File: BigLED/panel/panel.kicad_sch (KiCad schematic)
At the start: 29 parts, among them J1 Power, J2 LED PWR, J3 BTN1, J4 BTN2, J5 Spkr, U2 DAC7311xDCK, U3 NS4110B_C5334145

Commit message: Finist SCH for BigLED
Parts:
- added C12: 10.0, symbol Device:C
- added C13: 220x16v, symbol Device:C_Polarized
- added R5: 121, symbol Device:R
- added R6: 330, symbol Device:R
- added U4: LM1085-ADJ, symbol Regulator_Linear:LM1085-ADJ
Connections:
- net +3.3V: now also C13.1, R5.1, U4.2 (VO); no longer U1.2 (3Vo)
- net +5V: now also C12.1, U4.3 (VI)
- net GND: now also C12.2, C13.2, R6.2
- new net: R5.2, R6.1, U4.1 (ADJ)
- no-connect marks 0 -> 2

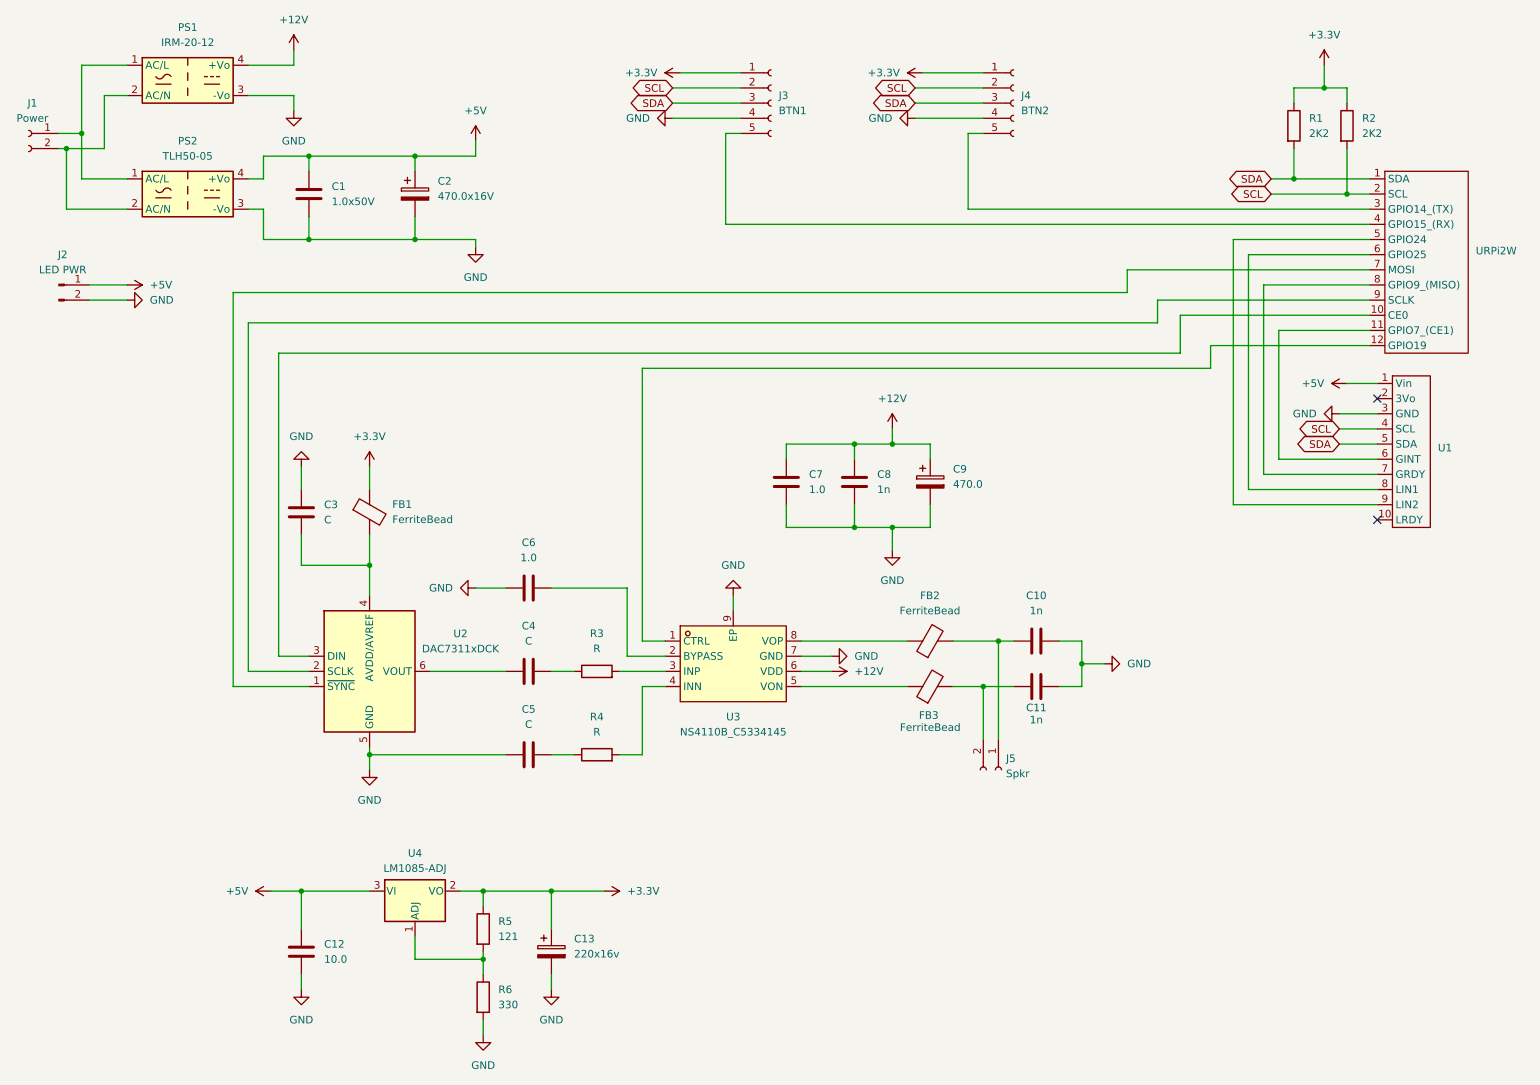
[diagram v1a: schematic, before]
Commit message: Converted BigLED to KiCAD v9
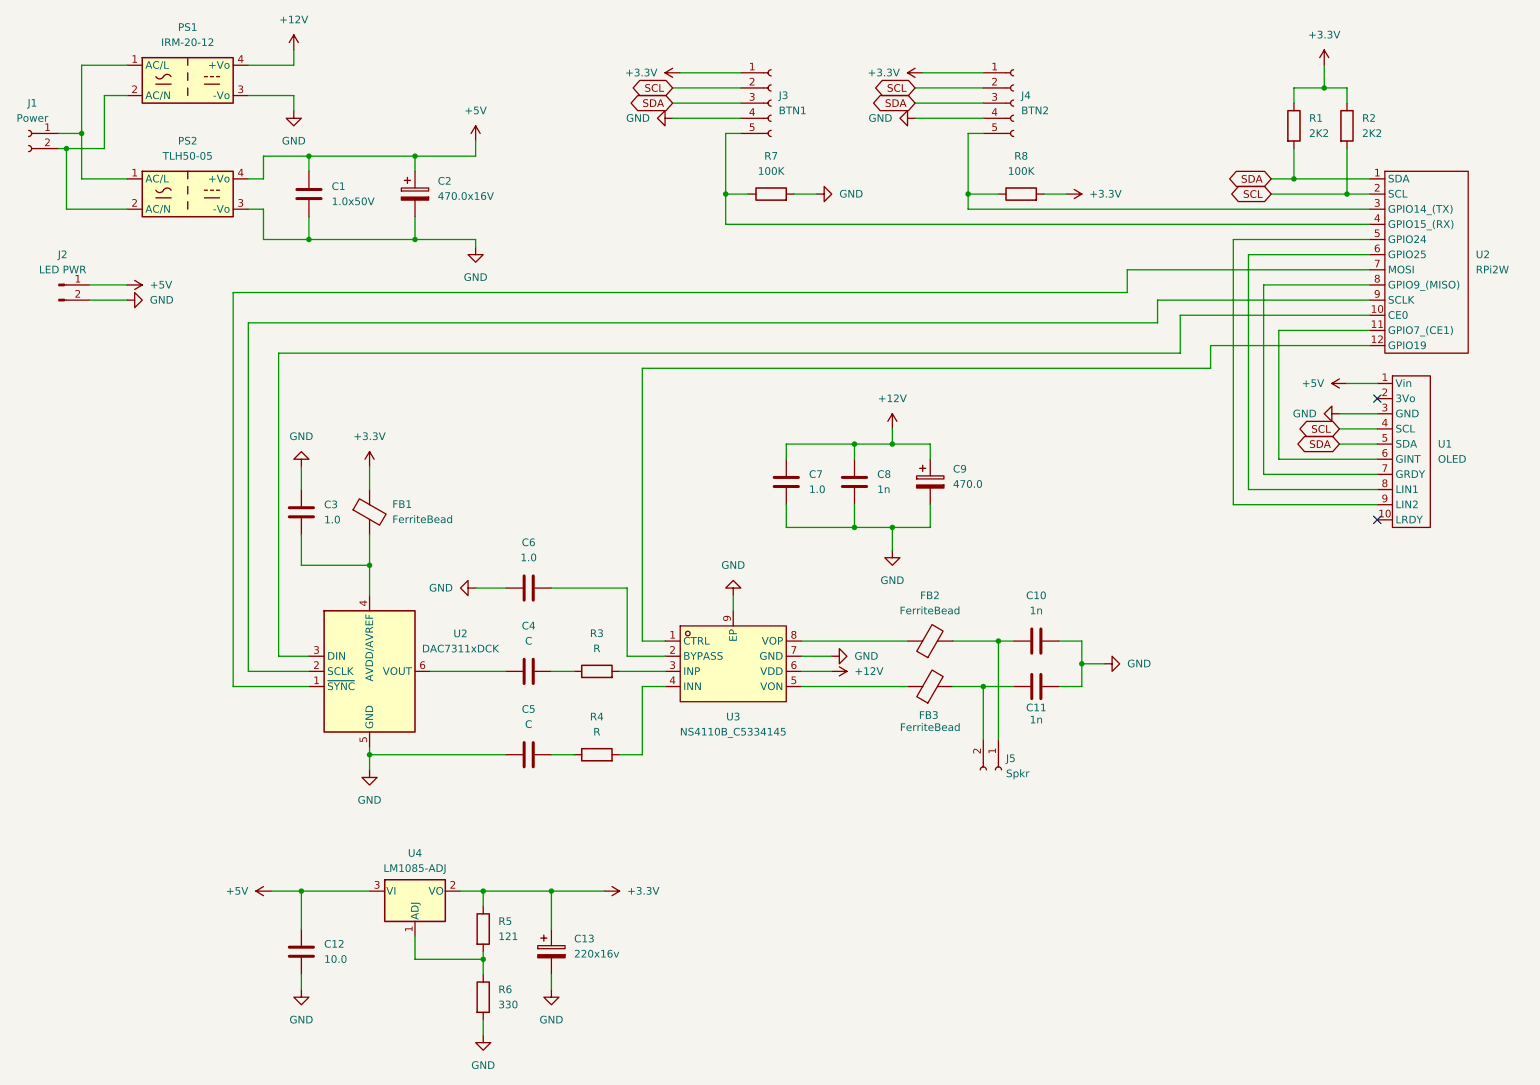
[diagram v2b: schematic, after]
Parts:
- added R7, R8: 100K, symbol Device:R
- C3: value C -> 1.0
- U1: value ~ -> OLED
- U2: renamed from URPi2W; value ~ -> RPi2W
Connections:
- net +3.3V: now also R8.2
- net GND: now also R7.2
- net at J3.5 (Pin_5), U2.4 (GPIO15_(RX)): now also R7.1
- net at J4.5 (Pin_5), U2.3 (GPIO14_(TX)): now also R8.1
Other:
- company: (none) -> RoboWay
- title: (none) -> BigLED

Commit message: Assigned packages for BigLED subprojects
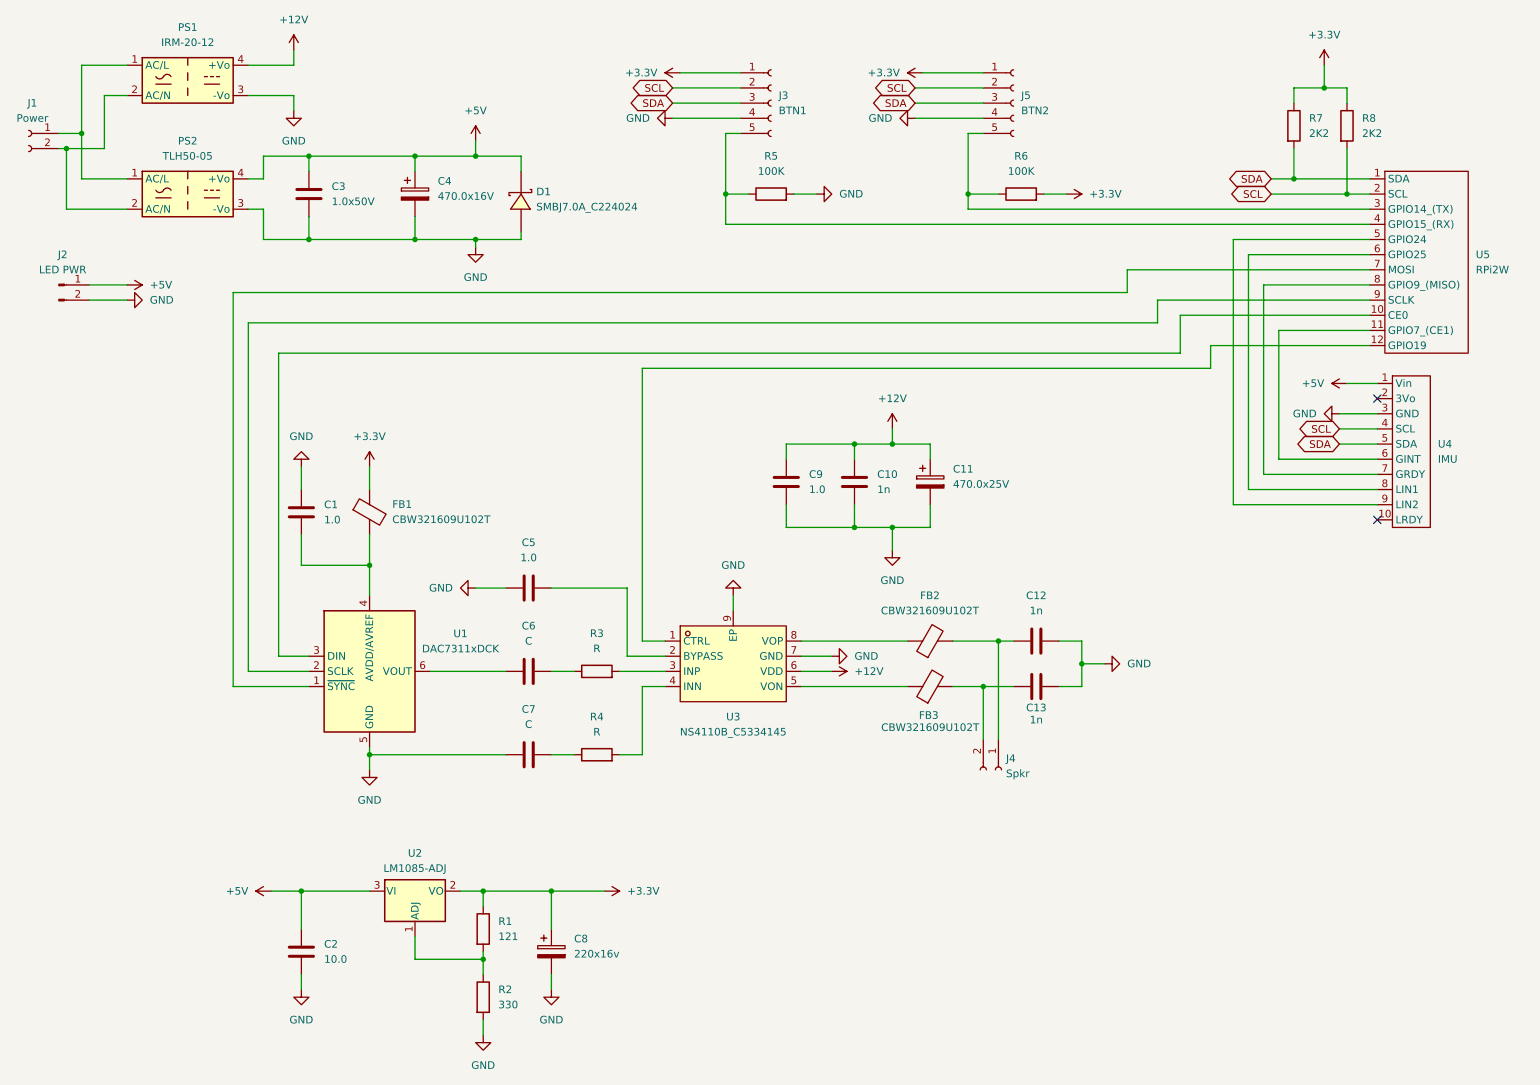
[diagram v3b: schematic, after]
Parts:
- added D1: SMBJ7.0A_C224024, easyeda2kicad:SMB_L4.6-W3.6-LS5.3-RD, symbol easyeda2kicad:SMBJ7.0A_C224024
- C1: renamed from C3; footprint (none) -> Capacitor_SMD:C_0603_1608Metric_Pad1.08x0.95mm_HandSolder
- C10: renamed from C8; footprint (none) -> Capacitor_SMD:C_0603_1608Metric_Pad1.08x0.95mm_HandSolder
- C11: renamed from C9; value 470.0 -> 470.0x25V; footprint (none) -> Capacitor_THT:CP_Radial_D8.0mm_P3.50mm
- C12: renamed from C10; footprint (none) -> Capacitor_SMD:C_0603_1608Metric_Pad1.08x0.95mm_HandSolder
- C13: renamed from C11; footprint (none) -> Capacitor_SMD:C_0603_1608Metric_Pad1.08x0.95mm_HandSolder
- C2: renamed from C12; footprint (none) -> Capacitor_SMD:C_1206_3216Metric_Pad1.33x1.80mm_HandSolder
- C3: renamed from C1; footprint (none) -> Capacitor_SMD:C_0603_1608Metric_Pad1.08x0.95mm_HandSolder
- C4: renamed from C2; footprint (none) -> Capacitor_THT:CP_Radial_D8.0mm_P3.50mm
- C5: renamed from C6; footprint (none) -> Capacitor_SMD:C_0603_1608Metric_Pad1.08x0.95mm_HandSolder
- C6: renamed from C4; footprint (none) -> Capacitor_SMD:C_0603_1608Metric_Pad1.08x0.95mm_HandSolder
- C7: renamed from C5; footprint (none) -> Capacitor_SMD:C_0603_1608Metric_Pad1.08x0.95mm_HandSolder
- C8: renamed from C13; footprint (none) -> Capacitor_THT:CP_Radial_D6.3mm_P2.50mm
- C9: renamed from C7; footprint (none) -> Capacitor_SMD:C_0603_1608Metric_Pad1.08x0.95mm_HandSolder
- FB1, FB2, FB3: value FerriteBead -> CBW321609U102T; footprint (none) -> easyeda2kicad:L1206
- J1: footprint (none) -> easyeda2kicad:CONN-TH_HAA420A-2A
- J2: footprint (none) -> Connector_JST:JST_XH_B2B-XH-A_1x02_P2.50mm_Vertical
- J3: footprint (none) -> Connector_JST:JST_XH_B5B-XH-A_1x05_P2.50mm_Vertical
- J4: renamed from J5; footprint (none) -> Connector_JST:JST_XH_B2B-XH-A_1x02_P2.50mm_Vertical
- J5: renamed from J4; footprint (none) -> Connector_JST:JST_XH_B5B-XH-A_1x05_P2.50mm_Vertical
- PS2: footprint Converter_ACDC:Converter_ACDC_MeanWell_IRM-20-xx_THT -> local:TLH50-23B
- R1: renamed from R5; footprint (none) -> Resistor_SMD:R_0603_1608Metric_Pad0.98x0.95mm_HandSolder
- R2: renamed from R6; footprint (none) -> Resistor_SMD:R_0603_1608Metric_Pad0.98x0.95mm_HandSolder
- R3, R4: footprint (none) -> Resistor_SMD:R_0603_1608Metric_Pad0.98x0.95mm_HandSolder
- R5: renamed from R7; footprint (none) -> Resistor_SMD:R_0603_1608Metric_Pad0.98x0.95mm_HandSolder
- R6: renamed from R8; footprint (none) -> Resistor_SMD:R_0603_1608Metric_Pad0.98x0.95mm_HandSolder
- R7: renamed from R1; footprint (none) -> Resistor_SMD:R_0603_1608Metric_Pad0.98x0.95mm_HandSolder
- R8: renamed from R2; footprint (none) -> Resistor_SMD:R_0603_1608Metric_Pad0.98x0.95mm_HandSolder
- U2: renamed from U4; footprint (none) -> local:TO-263-3_TabPin2
- U3: footprint easyeda2kicad:ESOP-8_L4.9-W3.9-P1.27-LS6.0-BL-EP-1 -> local:ESOP-8_L4.9-W3.9-P1.27-LS6.0-BL-EP-1-vias
- U4: renamed from U1; value OLED -> IMU; footprint (none) -> local:IMU9
- U5: renamed from U2; footprint (none) -> local:CONN-TH_XAD-12AS
- renumbered U2 to U1
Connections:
- net +5V: now also D1.1 (K)
- net GND: now also D1.2 (A)

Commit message: PCB for BigLED Panel started
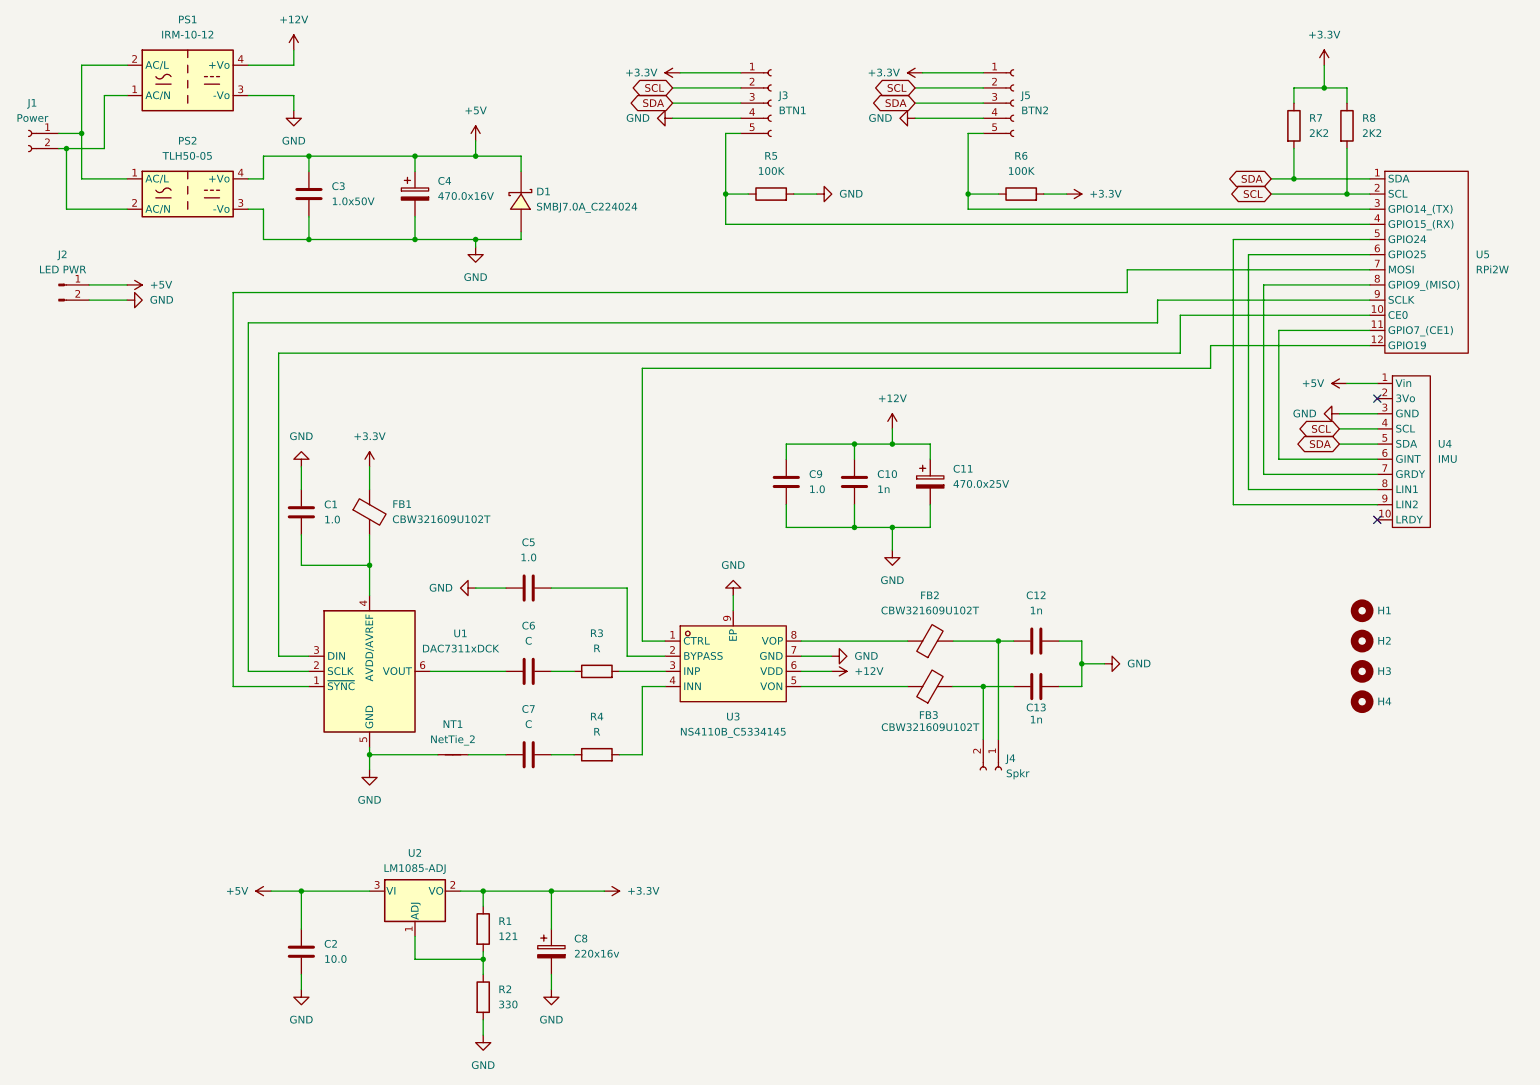
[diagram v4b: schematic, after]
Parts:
- removed PS1: IRM-20-12, Converter_ACDC:Converter_ACDC_MeanWell_IRM-20-xx_THT, symbol Converter_ACDC:IRM-20-12
- added H1, H2, H3, H4: MountingHole, MountingHole:MountingHole_3.2mm_M3, symbol Mechanical:MountingHole
- added NT1: NetTie_2, NetTie:NetTie-2_SMD_Pad0.5mm, symbol Device:NetTie_2
- added PS1: IRM-10-12, Converter_ACDC:Converter_ACDC_MeanWell_IRM-10-xx_THT, symbol Converter_ACDC:IRM-10-12
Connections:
- net +12V: now also PS1.4 (+Vo)
- net GND: now also NT1.1, PS1.3 (-Vo); no longer C7.1
- net at J1.1 (Pin_1), PS2.1 (AC/L): now also PS1.2 (AC/L)
- net at J1.2 (Pin_2), PS2.2 (AC/N): now also PS1.1 (AC/N)
- new net: C7.1, NT1.2

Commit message: Started BigLED master assemble draw
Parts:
- C6, C7: value C -> 82n
- R3, R4: value R -> 39K
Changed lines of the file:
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@@
 			)
 		)
-		(property "Value" "R"
+		(property "Value" "39K"
 			(at 113.03 125.73 90)
 			(effects
@@
 			)
 		)
-		(property "Value" "R"
+		(property "Value" "39K"
 			(at 113.03 139.7 90)
 			(effects
@@
 			)
 		)
-		(property "Value" "C"
+		(property "Value" "82n"
 			(at 101.6 124.46 90)
 			(effects
@@
 			)
 		)
-		(property "Value" "C"
+		(property "Value" "82n"
 			(at 101.6 138.43 90)
 			(effects
